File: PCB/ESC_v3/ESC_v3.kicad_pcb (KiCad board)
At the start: 4 copper layers, 42 x 83.5 mm, 137 parts, among them J1 Conn_01x04_Pin, J10 Conn_01x01_Pin, J11 Screw_Terminal_01x01, J2 Screw_Terminal_01x01, J3 Conn_01x01_Pin, J4 Conn_01x01_Pin, J5 Conn_01x01_Pin, J6 Conn_01x01_Pin, J7 Conn_01x01_Pin, J8 Conn_01x01_Pin, J9 Conn_01x01_Pin, Q1 NTMFS2D1N08XT1G, Q2 NTMFS2D1N08XT1G, Q3 NTMFS2D1N08XT1G, Q4 NTMFS2D1N08XT1G, Q5 NTMFS2D1N08XT1G, Q6 NTMFS2D1N08XT1G, U1 SN65HVD232, U2 DRV8323SRTAT, U5 STM32G431CBT6, Y2 24MHz

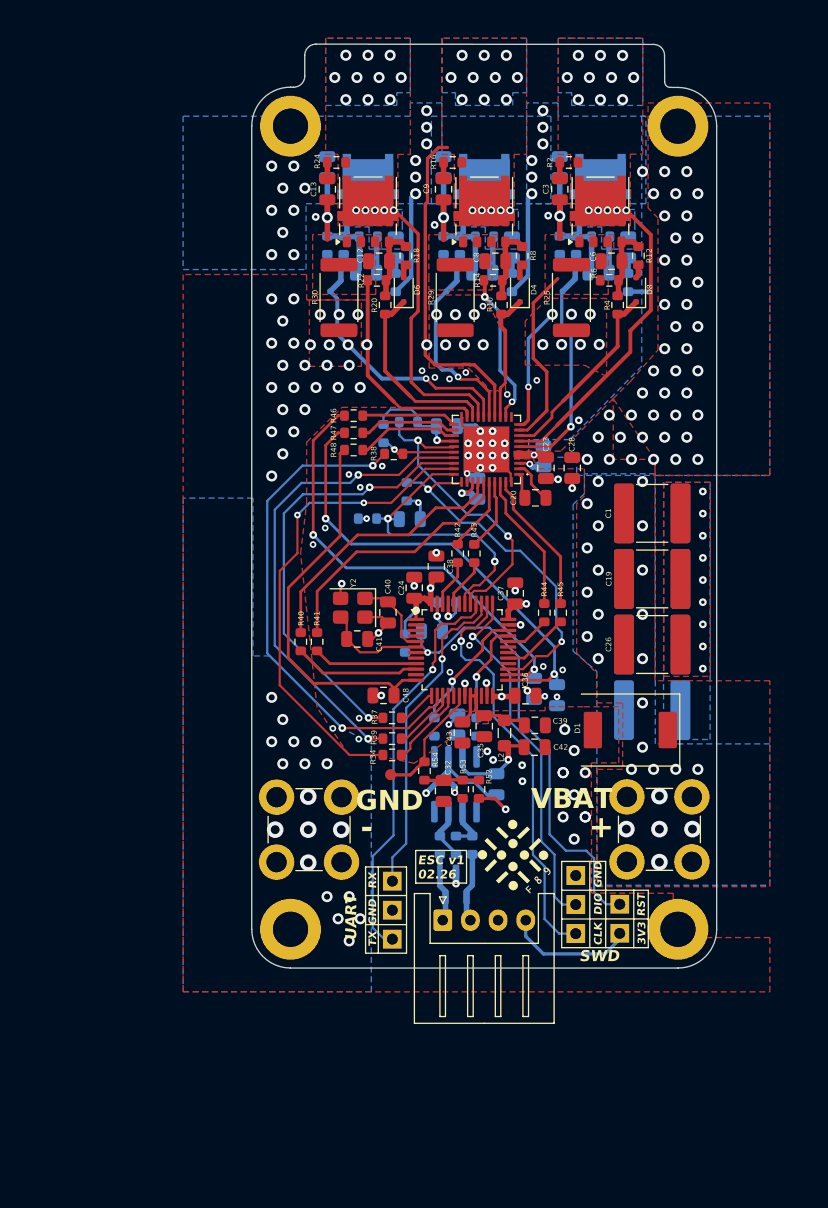
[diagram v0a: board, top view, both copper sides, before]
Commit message: Update DRVR schematic: relabels, wiring, net-ties
Refactor PCB/ESC_v3/DRVR.kicad_sch: cleaned up stray rectangles and comment text, repositioned many junctions and wires to fix connectivity, replaced/added global labels (reorganized SNA/SPA/SPB/SPC/SNB/SNC/etc.), and inserted NetTie symbols (NT1/NT3) with footprints to implement net ties. Updated symbol positions and UUIDs and removed obsolete schematic elements. Also touched top-level ESC_v3 files (ESC_v3.kicad_pcb, ESC_v3.kicad_prl, ESC_v3.kicad_sch, MCU.kicad_sch) and added/removed several backup archives.
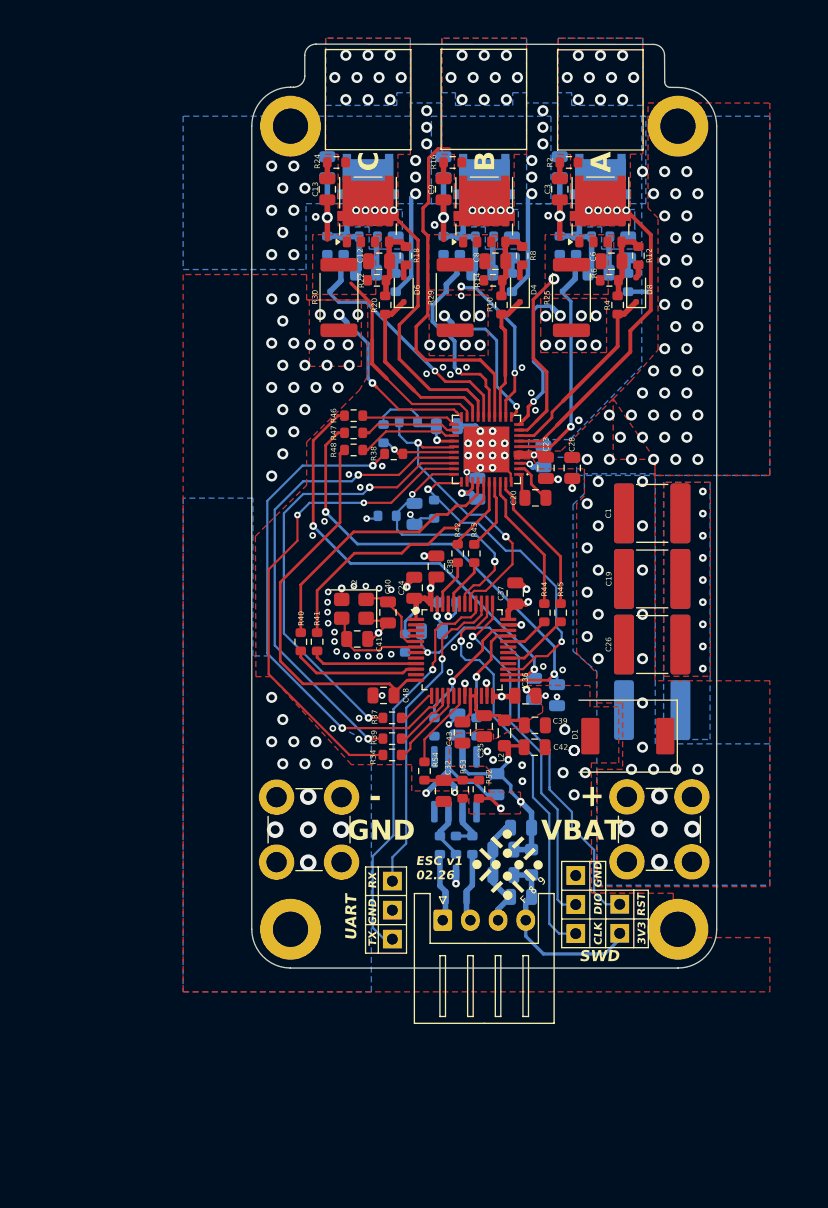
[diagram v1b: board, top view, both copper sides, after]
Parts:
- removed ?: , 
- added C44: 100n, Capacitor_SMD:C_0805_2012Metric, B.Cu at (148.5, 107.0)
- added C45: 22n, Capacitor_SMD:C_0805_2012Metric, B.Cu at (146.9, 105.0)
- added C49: 22n, Capacitor_SMD:C_0805_2012Metric, B.Cu at (146.9, 102.8)
- added C50: 100n, Capacitor_SMD:C_0805_2012Metric, B.Cu at (148.5, 100.8)
- added L1: 6.8uH, Inductor_SMD:L_0805_2012Metric_Pad1.05x1.20mm_HandSolder, B.Cu at (149.5, 103.9)
- added NT1: NetTie_2, NetTie:NetTie-2_SMD_Pad0.5mm, B.Cu at (151.7, 54.2)
- added NT2: NetTie_2, NetTie:NetTie-2_SMD_Pad0.5mm, B.Cu at (141.9, 54.9)
- added NT3: NetTie_2, NetTie:NetTie-2_SMD_Pad0.5mm, B.Cu at (132.4, 54.8)
- moved R31 2.93 mm to (140.7, 72.0)
- moved R26 1.79 mm to (136.4, 72.6)
- moved G*** 1.01 mm to (147.4, 104.2)
- moved C34 0.64 mm to (138.9, 72.4), turned to -90 degrees
- moved D1 0.59 mm to (158.6, 92.5)
- moved Y2 0.14 mm to (133.4, 81.0)
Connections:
- net VDDA renamed VREF
- C16 pad 1: VDD -> +3V3
- C17 pad 1: VDD -> +3V3
- C21 pad 1: VDD -> +3V3
- C24 pad 2: VDD -> +3V3
- C25 pad 1: VDD -> +3V3
- C36 pad 2: VDD -> +3V3
- C37 pad 2: VDD -> +3V3
- C38 pad 2: VDD -> +3V3
- C42 pad 2: VDD -> +3V3
- J1 pad 4: VDD -> +3V3RAW
- J4 pad 1: VDD -> +3V3RAW
- L2 pad 2: VDD -> +3V3
- R25 pad 2: SNA -> GND
- R26 pad 2: VDD -> +3V3
- R27 pad 2: VDD -> +3V3
- R28 pad 2: VDD -> +3V3
- R29 pad 2: SNB -> GND
- R30 pad 2: SNC -> GND
- R36 pad 1: VDD -> +3V3
- U1 pad 3: VDD -> +3V3
- U2 pad 24: VDD -> +3V3
- U2 pad 33: VDD -> +3V3
- U5 pad 1: VDD -> +3V3
- U5 pad 24: VDD -> +3V3
- U5 pad 36: VDD -> +3V3
- U5 pad 48: VDD -> +3V3
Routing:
- net VDD: track 126.6 -> 0.00 mm, vias 8 -> 0
- net +3V3: track 0.00 -> 113.6 mm, vias 0 -> 9
- net +3V3RAW: track 0.00 -> 17.6 mm
- net SNC: track 0.00 -> 15.7 mm, vias 0 -> 1
- net SNB: track 0.00 -> 12.5 mm, vias 0 -> 1
- net GND: track 54.2 -> 60.9 mm, vias 139 -> 146
- net V_BAT_MEAS: track 10.8 -> 7.36 mm
- net ENABLE: track 27.3 -> 24.6 mm
- net CAL: track 31.7 -> 29.5 mm
- net SNA: track 11.5 -> 13.5 mm
- net V_B_PHASE: track 33.6 -> 35.6 mm
- net V_C_PHASE: track 30.7 -> 32.5 mm
- net G_C_H: track 25.2 -> 23.7 mm
- net NRST: track 43.4 -> 42.4 mm
- net SPB: track 21.0 -> 22.1 mm
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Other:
- board text added: "A"
- board text added: "B"
- board text added: "C"

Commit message: ESC_v3: footprint, PCB teardrops & backup updates
Remove Notes.txt; update ESC_v3 PCB and schematic files. In DRVR.kicad_sch several capacitor footprints changed from 0805 to 0603. ESC_v3.kicad_pcb: set grid_origin, added teardrops to multiple pads, updated many component UUIDs and silkscreen font thicknesses, and other layout metadata tweaks. Clean up old ESC_v3 backup zips and add new timestamped backup archives. Also update related KiCad project files (.kicad_prl, .kicad_pro). These changes shrink component footprints, improve manufacturability (teardrops), and refresh project backups/metadata.
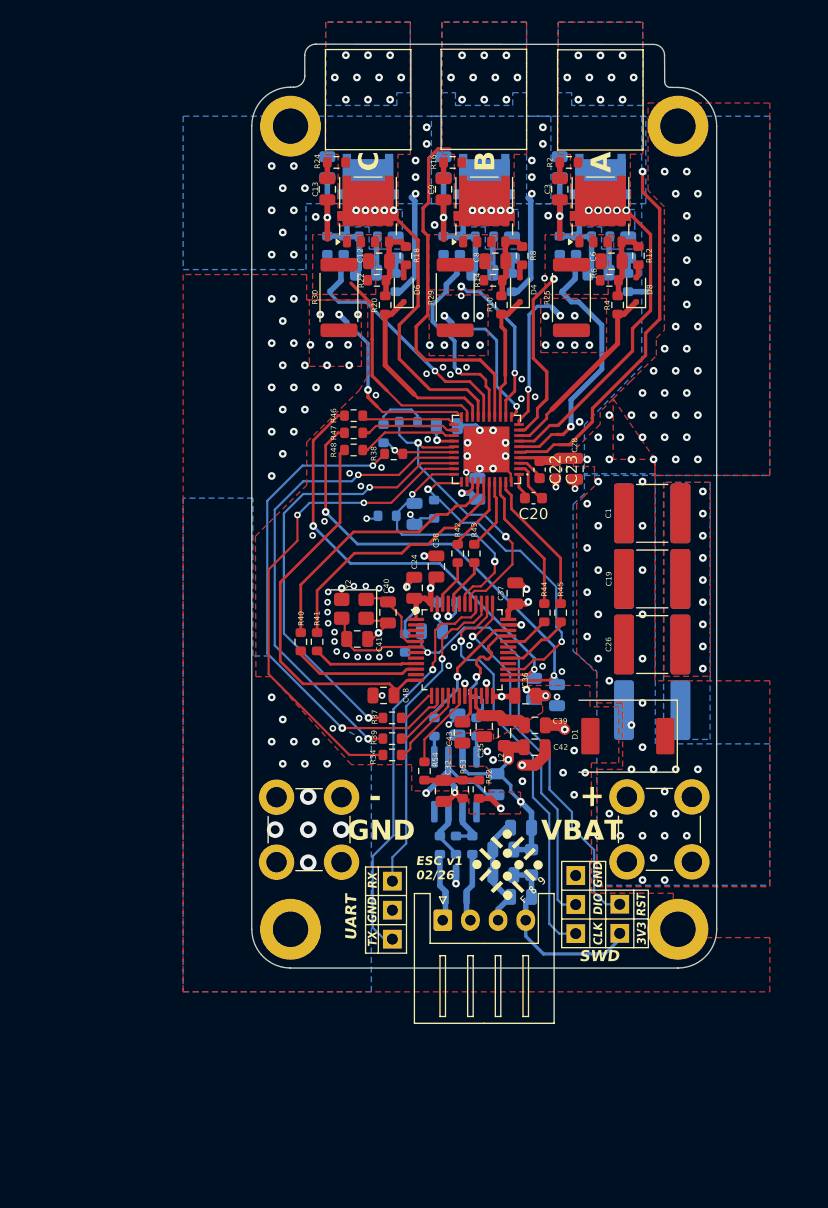
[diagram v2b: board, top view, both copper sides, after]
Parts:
- C20, C23: footprint Capacitor_SMD:C_0805_2012Metric -> Capacitor_SMD:C_0603_1608Metric
- C22: footprint Capacitor_SMD:C_0805_2012Metric -> Capacitor_SMD:C_0603_1608Metric; moved to F.Cu
- moved C22 1.25 mm to (150.2, 68.4)
- moved C23 0.91 mm to (151.7, 68.4)
- moved C28 0.26 mm to (153.4, 68.3)
- moved C20 0.18 mm to (149.7, 71.0)
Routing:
- net V_BAT: track 45.4 -> 82.4 mm, vias 90 -> 92
- net GND: track 60.9 -> 68.8 mm, vias 146 -> 143
- net Net-(C32-Pad1): track 4.97 -> 8.18 mm
- net G_A_H: track 21.9 -> 24.6 mm
- net CAN_RX: track 9.18 -> 11.7 mm
- net Net-(U1-R): track 0.00 -> 1.88 mm
- net Net-(U1-D): track 0.00 -> 1.88 mm
- net SNC: track 15.7 -> 16.7 mm
- net G_A_L: track 18.2 -> 17.4 mm
- net SNA: track 13.5 -> 12.8 mm
- net SPC: track 26.1 -> 26.7 mm
- net Net-(U2-VCP): track 2.73 -> 2.54 mm, vias 1 -> 0
- added copper zone on In2.Cu, net V_A_PHASE
- added copper zone on In2.Cu, net V_B_PHASE
- added copper zone on In2.Cu, net V_C_PHASE
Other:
- board text added: "ESC v1 02/26"
- board text removed: "ESC v1 02.26"

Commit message: STM changed
Changed specific STM model for better pinouts and layout
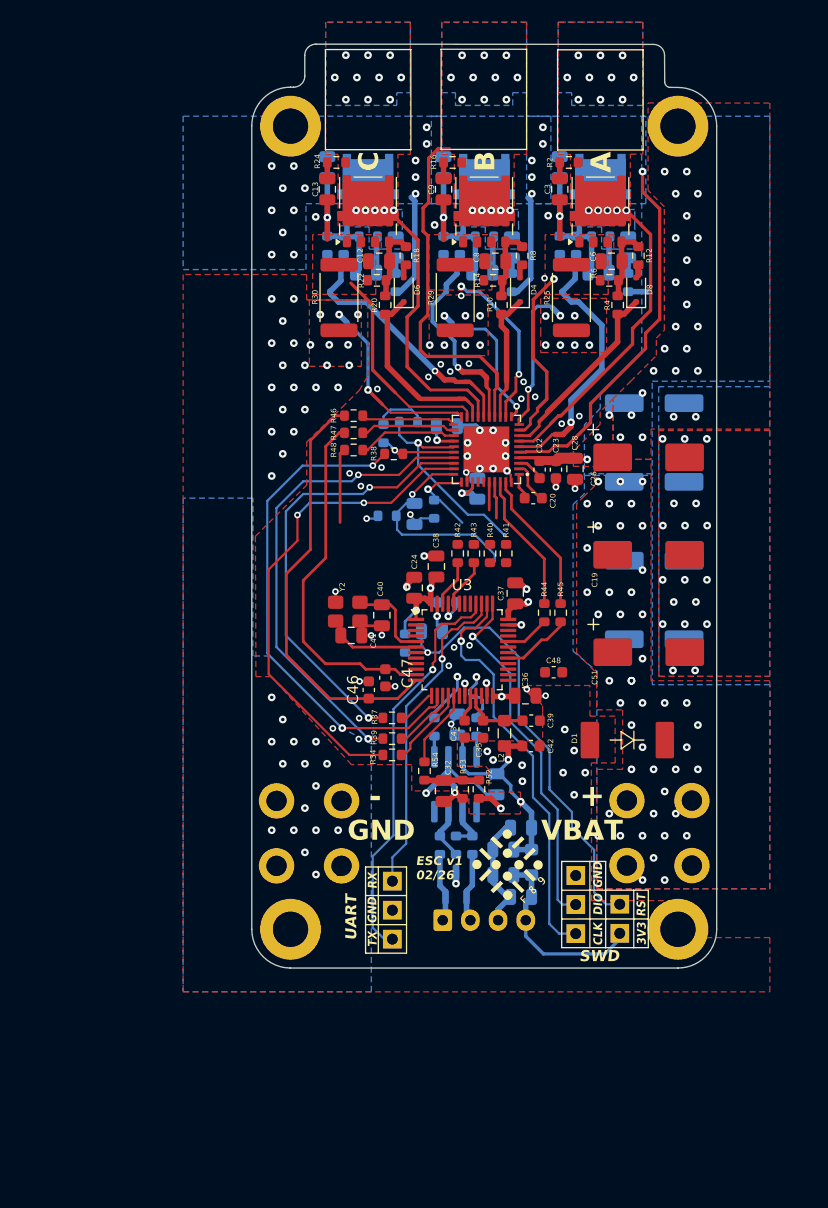
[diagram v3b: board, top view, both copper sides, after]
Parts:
- removed C1: 100-220uF, Capacitor_SMD:C_2220_5750Metric
- removed U5: STM32G431CBT6, Package_QFP:LQFP-48_7x7mm_P0.5mm
- added C51: 100-220uF, Capacitor_SMD:CP_Elec_8x10, F.Cu at (160.1, 84.9)
- added U3: STM32G474CETx, Package_QFP:LQFP-48_7x7mm_P0.5mm, F.Cu at (143.2, 84.7)
- C19, C26: footprint Capacitor_SMD:C_2220_5750Metric -> Capacitor_SMD:CP_Elec_8x10
- C27, C29, C30, C31: footprint Capacitor_SMD:C_2220_5750Metric -> Capacitor_SMD:CP_Elec_6.3x7.7
- C35, C39, C42, C43, C48: footprint Capacitor_SMD:C_0805_2012Metric -> Capacitor_SMD:C_0603_1608Metric
- C46, C47: footprint Capacitor_SMD:C_0805_2012Metric -> Capacitor_SMD:C_0603_1608Metric; moved to F.Cu
- moved C27 27.7 mm to (160.6, 62.4)
- moved R40 18.9 mm to (145.7, 76.0)
- moved R41 18.9 mm to (147.2, 76.0)
- moved C26 16.9 mm to (160.1, 67.3)
- moved C47 15.6 mm to (136.3, 87.2)
- moved C48 15.5 mm to (151.5, 86.7), turned to 0 degrees
- moved C46 14.9 mm to (134.8, 88.3), turned to 90 degrees
- moved C31 2.85 mm to (160.6, 69.5)
- moved C19 2.20 mm to (160.1, 76.1)
- moved C30 1.66 mm to (160.6, 76.7)
- moved C41 0.62 mm to (133.2, 83.4)
- moved C40 0.61 mm to (135.9, 81.6)
- moved Y2 0.61 mm to (132.9, 81.3)
- moved C39 0.54 mm to (149.4, 91.1)
- moved C29 0.51 mm to (160.6, 83.8)
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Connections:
- net ADC1_IN11 renamed ADC2_IN17
- net ADC1_IN14 renamed ADC1_IN4
- net ADC2_IN12 renamed ADC4_IN4
- R40 pad 1: INHA -> INHB
- R40 pad 2: TIM15_CH1 -> TIM8_CH1
- R41 pad 1: INLA -> INLB
- R41 pad 2: TIM15_CH1N -> TIM8_CH1N
- R42 pad 1: INHB -> INHA
- R43 pad 1: INLB -> INLA
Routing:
- net ADC4_IN4: track 35.9 -> 6.76 mm
- net INHA: track 24.8 -> 0.00 mm
- net INLA: track 23.9 -> 0.00 mm
- net CAL: track 29.8 -> 7.91 mm, vias 2 -> 1
- net TIM15_CH1: track 11.9 -> 0.00 mm
- net ADC1_IN4: track 41.8 -> 32.1 mm, vias 2 -> 0
- net TIM15_CH1N: track 9.46 -> 0.00 mm
- net NFAULT: track 27.7 -> 19.2 mm, vias 2 -> 1
- net CAN_TX: track 11.3 -> 4.58 mm
- net CAN_RX: track 11.7 -> 5.07 mm
- net GND: track 68.8 -> 62.2 mm, vias 143 -> 141
- net ENABLE: track 24.7 -> 19.3 mm, vias 2 -> 1
- net INHB: track 6.82 -> 2.55 mm
- net INLB: track 6.54 -> 3.34 mm
- net ADC2_IN17: track 40.6 -> 38.3 mm, vias 2 -> 0
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
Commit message: Layout edit
Changed some layout and optimized
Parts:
- C24: footprint Capacitor_SMD:C_0805_2012Metric -> Capacitor_SMD:C_0603_1608Metric
- C48: footprint Capacitor_SMD:C_0603_1608Metric -> Capacitor_SMD:C_0805_2012Metric
- moved NT2 2.57 mm to (144.2, 53.5), turned to 180 degrees
- moved C15 2.38 mm to (141.2, 43.5)
- moved C18 2.32 mm to (130.7, 43.4)
- moved C4 2.24 mm to (151.6, 43.3)
- moved NT3 1.20 mm to (132.6, 53.6)
- moved NT1 1.09 mm to (151.2, 53.2), turned to 0 degrees
- moved C48 0.97 mm to (150.5, 86.5)
- moved C33 0.73 mm to (139.8, 83.2), turned to 90 degrees
- moved R40 0.71 mm to (145.0, 76.0)
- moved R41 0.71 mm to (146.5, 76.0)
- moved R42 0.71 mm to (142.1, 76.0)
- moved R43 0.71 mm to (143.6, 76.0)
- moved C38 0.52 mm to (140.4, 77.3)
- moved C24 0.38 mm to (138.7, 79.4)
- moved C41 0.36 mm to (133.3, 83.8)
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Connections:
- U3 pad 33: unconnected-(U3-PA11-Pad33) -> NFAULT
- U3 pad 34: unconnected-(U3-PA12-Pad34) -> ENABLE
- U3 pad 39: unconnected-(U3-PA15-Pad39) -> CAL
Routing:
- net ADC4_IN4: track 6.76 -> 35.8 mm, vias 0 -> 2
- net CAL: track 7.91 -> 20.5 mm, vias 1 -> 2
- net NFAULT: track 19.2 -> 30.8 mm, vias 1 -> 2
- net ENABLE: track 19.3 -> 29.0 mm, vias 1 -> 2
- net USART2_TX: track 36.5 -> 28.7 mm
- net SPA: track 27.5 -> 20.3 mm, vias 2 -> 1
- net INHA: track 0.00 -> 6.69 mm
- net INLA: track 0.00 -> 6.29 mm
- net CAN_TX: track 4.58 -> 9.39 mm
- net TIM8_CH1: track 0.00 -> 4.58 mm
- net TIM8_CH1N: track 0.00 -> 4.56 mm
- net GND: track 62.2 -> 66.7 mm, vias 141 -> 140
- net NRST: track 42.4 -> 38.9 mm
- net INHB: track 2.55 -> 5.90 mm
- net CAN_RX: track 5.07 -> 7.83 mm
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
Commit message: Layout update
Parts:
- added J1: Conn_01x02_Pin, Connector_AMASS:AMASS_XT60PW-M_1x02_P7.20mm_Horizontal, F.Cu at (133.4, 116.6)
- added U1: SN65HVD232, Package_SO:SOIC-8_3.9x4.9mm_P1.27mm, F.Cu at (110.8, 108.2)
- added U4: TCAN334G, Package_SO:JEITA_SOIC-8_3.9x4.9mm_P1.27mm, F.Cu at (107.5, 101.1)
- added U5: TCAN334G, Package_SO:SOIC-8_3.9x4.9mm_P1.27mm, F.Cu at (107.6, 94.5)
- added U6: TCAN334G, Package_TO_SOT_SMD:TSOT-23-8, F.Cu at (114.3, 100.1)
- added U7: SN65HVD232, Package_SO:SOIC-8_3.9x4.9mm_P1.27mm, F.Cu at (106.9, 86.8)
- R51: value DNP -> 120R/DNP
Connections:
- R51 pad 1: Net-(U1-CANL) -> CAN_L
- R51 pad 2: Net-(U1-CANH) -> CAN_H
- U1 pad 1: Net-(U1-D) -> CAN_TX
- U1 pad 4: Net-(U1-R) -> CAN_RX
- U1 pad 6: Net-(U1-CANL) -> CAN_L
- U1 pad 7: Net-(U1-CANH) -> CAN_H

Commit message: Layout update
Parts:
- removed C49: 22n, Capacitor_SMD:C_0805_2012Metric
- removed C50: 100n, Capacitor_SMD:C_0805_2012Metric
- removed L1: 6.8uH, Inductor_SMD:L_0805_2012Metric_Pad1.05x1.20mm_HandSolder
- removed R32, R33, R49, R50: 22Ω, Resistor_SMD:R_0603_1608Metric
- removed the U1 at (110.8, 108.2)
- removed U4: TCAN334G, Package_SO:JEITA_SOIC-8_3.9x4.9mm_P1.27mm
- removed U5: TCAN334G, Package_SO:SOIC-8_3.9x4.9mm_P1.27mm
- removed U6: TCAN334G, Package_TO_SOT_SMD:TSOT-23-8
- removed U7: SN65HVD232, Package_SO:SOIC-8_3.9x4.9mm_P1.27mm
- added C1: 1-4u7, Capacitor_SMD:C_0805_2012Metric, B.Cu at (148.5, 105.2)
- added IC1: TLV77333PDBVR, SamacSys_Parts:SOT95P280X145-5N, B.Cu at (148.5, 102.1)
- C44: value 100n -> DNP
- C45: value 22n -> 1u
- moved C45 6.46 mm to (148.8, 98.8), turned to 180 degrees
- moved C17 1.51 mm to (145.8, 98.3)
- moved U1 1.51 mm to (142.1, 98.3)
- moved C16 1.51 mm to (142.3, 92.9)
- moved R51 0.86 mm to (142.1, 103.0), turned to 180 degrees
- moved D9 0.45 mm to (142.2, 105.9)
- moved C44 0.36 mm to (148.2, 107.2), turned to 180 degrees
- moved C32 0.15 mm to (141.5, 97.3)
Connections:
- C44 pad 1: GND -> +5V
- C44 pad 2: +3V3RAW -> GND
- C45 pad 1: GND -> +3V3
- C45 pad 2: +3V3RAW -> GND
- J1 pad 4: +3V3RAW -> +5V
- J3 pad 1: GND -> SWDIO
- J4 pad 1: +3V3RAW -> GND
- J5 pad 1: SWCLK -> +3V3
- J6 pad 1: SWDIO -> SWCLK
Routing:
- net +3V3RAW: track 17.6 -> 0.00 mm
- net GND: track 66.7 -> 56.3 mm, vias 140 -> 139
- net +3V3: track 111.0 -> 118.6 mm
- net CAN_TX: track 9.39 -> 14.5 mm
- net Net-(U1-CANH): track 4.97 -> 0.00 mm
- net Net-(U1-CANL): track 4.04 -> 0.00 mm
- net +5V: track 0.00 -> 3.87 mm
- net CAN_RX: track 7.83 -> 11.6 mm
- net SWDIO: track 32.9 -> 29.6 mm
- net SWCLK: track 37.2 -> 34.3 mm
- net CAN_L: track 6.35 -> 9.16 mm
- net CAN_H: track 6.27 -> 8.76 mm
- net Net-(U1-R): track 1.88 -> 0.00 mm
- net Net-(U1-D): track 1.88 -> 0.00 mm
- added copper zone on B.Cu, net +3V3
- added copper zone on B.Cu, net +5V
